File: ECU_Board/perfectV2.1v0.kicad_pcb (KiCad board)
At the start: 4 copper layers, 100 x 100 mm, 170 parts, among them IC1 Trig Cond Socket, IC2 Trig Cond Socket, J1 Conn_02x20_Odd_Even, J2 Conn_01x02, J3 MAP_Connector, J4 Conn_01x06, J5 Conn_01x05, J6 Conn_01x05, J8 Conn_01x04, Q1 SSM3K318R, Q2 SSM3K318R, Q3 SSM3K318R, U1 Teensy4.1, U10 LM324A, U11 LM324A, U12 CD4504B, U13 CD4504B, U14 CD4504B, U2 LM2576-5G, U3 SP720, U4 BM2LC105, U5 BM2LC105, U6 TC4424A, U7 TC4424A, U8 BM2LC105, U9 BM2LC105

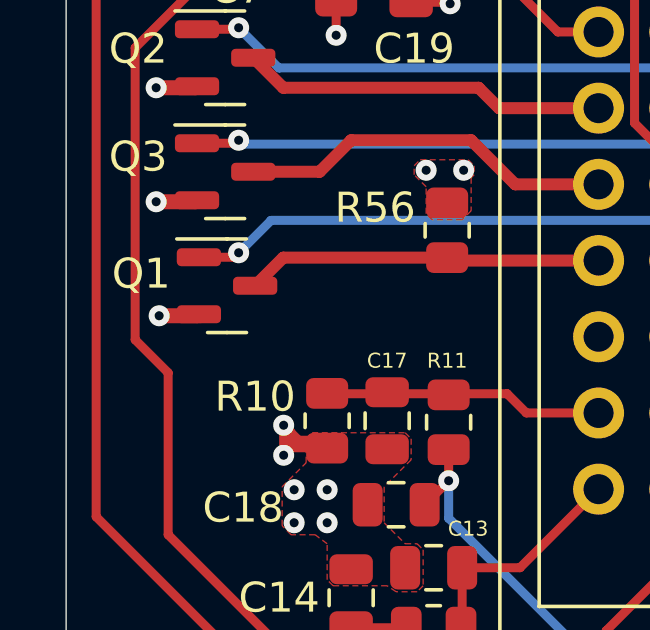
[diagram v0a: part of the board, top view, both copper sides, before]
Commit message: Changed Boost output to ACIS
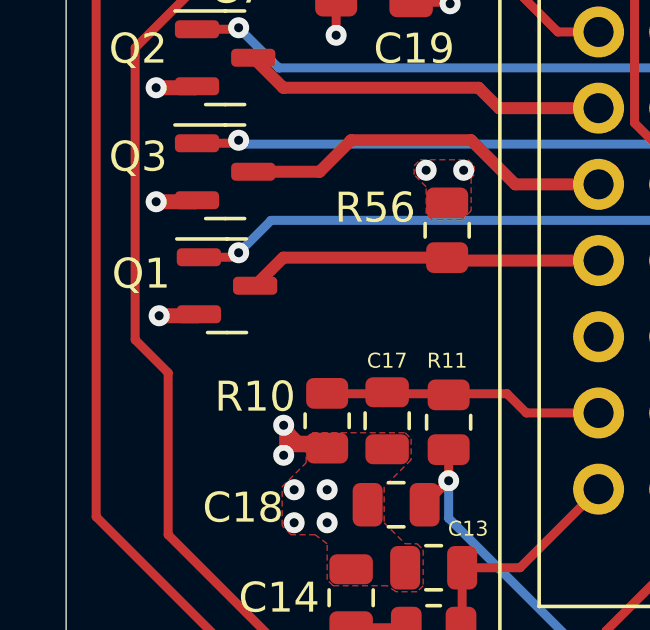
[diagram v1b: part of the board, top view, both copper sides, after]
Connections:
- net BOOST-5V renamed ACIS-5V
- net BOOST-OUT renamed ACIS-OUT
- net MCU-BOOST renamed MCU-ACIS
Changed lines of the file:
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@@
   (net 19 "BAT-5V")
   (net 20 "IDLE-OUT")
-  (net 21 "BOOST-OUT")
+  (net 21 "ACIS-OUT")
   (net 22 "CLT-5V")
   (net 23 "FLEX-IN")
@@
   (net 102 "MCU-IGN3")
   (net 103 "Net-(R46-Pad2)")
-  (net 104 "BOOST-5V")
+  (net 104 "ACIS-5V")
   (net 105 "Net-(R49-Pad1)")
   (net 106 "Net-(JP1-Pad2)")
@@
   (net 128 "MCU-INJ3")
   (net 129 "unconnected-(U1-Pad15)")
-  (net 130 "MCU-BOOST")
+  (net 130 "MCU-ACIS")
   (net 131 "unconnected-(U1-Pad18)")
   (net 132 "MCU-IDLE")
@@
       (net 2 "+12V") (pinfunction "K") (pintype "passive"))
     (pad "2" smd rect (at 1.65 0) (size 0.9 1.2) (layers "F.Cu" "F.Paste" "F.Mask")
-      (net 21 "BOOST-OUT") (pinfunction "A") (pintype "passive"))
+      (net 21 "ACIS-OUT") (pinfunction "A") (pintype "passive"))
     (model "${KICAD6_3DMODEL_DIR}/Diode_SMD.3dshapes/D_SOD-123.wrl"
       (offset (xyz 0 0 0))
@@
       (net 129 "unconnected-(U1-Pad15)") (pinfunction "3V3") (pintype "power_in+no_connect"))
     (pad "16" thru_hole circle (at 8.89 7.62 90) (size 1.6 1.6) (drill 1.1) (layers *.Cu *.Mask)
-      (net 130 "MCU-BOOST") (pinfunction "24_A10_TX6_SCL2") (pintype "bidirectional"))
+      (net 130 "MCU-ACIS") (pinfunction "24_A10_TX6_SCL2") (pintype "bidirectional"))
     (pad "17" thru_hole circle (at 11.43 7.62 90) (size 1.6 1.6) (drill 1.1) (layers *.Cu *.Mask)
       (net 79 "MCU-FAN") (pinfunction "25_A11_RX6_SDA2") (pintype "bidirectional"))
@@
       (net 105 "Net-(R49-Pad1)") (pintype "passive"))
     (pad "2" smd roundrect (at 0.51 0 270) (size 0.54 0.64) (layers "F.Cu" "F.Paste" "F.Mask") (roundrect_rratio 0.25)
-      (net 104 "BOOST-5V") (pintype "passive"))
+      (net 104 "ACIS-5V") (pintype "passive"))
     (model "${KICAD6_3DMODEL_DIR}/Resistor_SMD.3dshapes/R_0402_1005Metric.wrl"
       (offset (xyz 0 0 0))
@@
       (net 1 "GND") (pinfunction "SOURCE1") (pintype "input"))
     (pad "8" smd roundrect (at 2.625 -1.905 180) (size 1.65 0.6) (layers "F.Cu" "F.Paste" "F.Mask") (roundrect_rratio 0.25)
-      (net 21 "BOOST-OUT") (pinfunction "DRAIN1") (pintype "output"))
+      (net 21 "ACIS-OUT") (pinfunction "DRAIN1") (pintype "output"))
     (model "${KICAD6_3DMODEL_DIR}/Package_SO.3dshapes/SOP-8_3.9x4.9mm_P1.27mm.wrl"
       (offset (xyz 0 0 0))
@@
       (net 18 "INJ-4-OUT") (pinfunction "Pin_11") (pintype "passive"))
     (pad "12" thru_hole circle (at 2.54 12.7) (size 1.7 1.7) (drill 1) (layers *.Cu *.Mask)
-      (net 21 "BOOST-OUT") (pinfunction "Pin_12") (pintype "passive"))
+      (net 21 "ACIS-OUT") (pinfunction "Pin_12") (pintype "passive"))
     (pad "13" thru_hole circle (at 0 15.24) (size 1.7 1.7) (drill 1) (layers *.Cu *.Mask)
       (net 27 "IGN-1-OUT") (pinfunction "Pin_13") (pintype "passive"))
@@
       (net 33 "+3V3") (pinfunction "VCC") (pintype "power_in"))
     (pad "2" smd roundrect (at -2.8625 -1.625) (size 1.475 0.4) (layers "F.Cu" "F.Paste" "F.Mask") (roundrect_rratio 0.25)
-      (net 104 "BOOST-5V") (pinfunction "Aout") (pintype "output"))
+      (net 104 "ACIS-5V") (pinfunction "Aout") (pintype "output"))
     (pad "3" smd roundrect (at -2.8625 -0.975) (size 1.475 0.4) (layers "F.Cu" "F.Paste" "F.Mask") (roundrect_rratio 0.25)
-      (net 130 "MCU-BOOST") (pinfunction "Ain") (pintype "input"))
+      (net 130 "MCU-ACIS") (pinfunction "Ain") (pintype "input"))
     (pad "4" smd roundrect (at -2.8625 -0.325) (size 1.475 0.4) (layers "F.Cu" "F.Paste" "F.Mask") (roundrect_rratio 0.25)
       (net 85 "INJ1-5V") (pinfunction "Bout") (pintype "output"))
@@
     (fp_line (start -0.525 0.27) (end -0.525 -0.27) (layer "F.Fab") (width 0.1))
     (pad "1" smd roundrect (at -0.51 0 90) (size 0.54 0.64) (layers "F.Cu" "F.Paste" "F.Mask") (roundrect_rratio 0.25)
-      (net 104 "BOOST-5V") (pintype "passive"))
+      (net 104 "ACIS-5V") (pintype "passive"))
     (pad "2" smd roundrect (at 0.51 0 90) (size 0.54 0.64) (layers "F.Cu" "F.Paste" "F.Mask") (roundrect_rratio 0.25)
       (net 1 "GND") (pintype "passive"))
@@
   (segment (start 139 113.1) (end 139 111.45) (width 1) (layer "F.Cu") (net 1))
   (segment (start 88.21375 116.22) (end 87.22 116.22) (width 0.5) (layer "F.Cu") (net 1))
-  (segment (start 51.975 152.6) (end 51.925 152.55) (width 0.5) (layer "F.Cu") (net 1))
   (segment (start 74.75125 125.455) (end 75.80125 124.405) (width 0.3) (layer "F.Cu") (net 1))
   (segment (start 86.72 125.42) (end 86.7 125.4) (width 0.3) (layer "F.Cu") (net 1))

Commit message: Finished adapter board, slight changes to ECU
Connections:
- net FAN-OUT renamed HT-OUT
- net MCU-FAN renamed MCU-HT
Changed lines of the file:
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@@
   (net 77 "Net-(JP7-Pad3)")
   (net 78 "MCU-TACHO")
-  (net 79 "MCU-FAN")
-  (net 80 "FAN-OUT")
+  (net 79 "HT-OUT")
+  (net 80 "MCU-HT")
   (net 81 "FUELPUMP-OUT")
   (net 82 "MCU-PUMP")
@@
       (net 130 "MCU-ACIS") (pinfunction "24_A10_TX6_SCL2") (pintype "bidirectional"))
     (pad "17" thru_hole circle (at 11.43 7.62 90) (size 1.6 1.6) (drill 1.1) (layers *.Cu *.Mask)
-      (net 79 "MCU-FAN") (pinfunction "25_A11_RX6_SDA2") (pintype "bidirectional"))
+      (net 80 "MCU-HT") (pinfunction "25_A11_RX6_SDA2") (pintype "bidirectional"))
     (pad "18" thru_hole circle (at 13.97 7.62 90) (size 1.6 1.6) (drill 1.1) (layers *.Cu *.Mask)
       (net 131 "unconnected-(U1-Pad18)") (pinfunction "26_A12_MOSI1") (pintype "bidirectional+no_connect"))
@@
       (net 69 "VR1-") (pinfunction "Pin_28") (pintype "passive"))
     (pad "29" thru_hole circle (at 0 35.56) (size 1.7 1.7) (drill 1) (layers *.Cu *.Mask)
-      (net 80 "FAN-OUT") (pinfunction "Pin_29") (pintype "passive"))
+      (net 79 "HT-OUT") (pinfunction "Pin_29") (pintype "passive"))
     (pad "30" thru_hole circle (at 2.54 35.56) (size 1.7 1.7) (drill 1) (layers *.Cu *.Mask)
       (net 70 "VR2-") (pinfunction "Pin_30") (pintype "passive"))
@@
     (fp_line (start 0.65 1.45) (end -0.65 1.45) (layer "F.Fab") (width 0.1))
     (pad "1" smd roundrect (at -0.9375 -0.95) (size 1.475 0.6) (layers "F.Cu" "F.Paste" "F.Mask") (roundrect_rratio 0.25)
-      (net 79 "MCU-FAN") (pinfunction "G") (pintype "input"))
+      (net 80 "MCU-HT") (pinfunction "G") (pintype "input"))
     (pad "2" smd roundrect (at -0.9375 0.95) (size 1.475 0.6) (layers "F.Cu" "F.Paste" "F.Mask") (roundrect_rratio 0.25)
       (net 1 "GND") (pinfunction "S") (pintype "passive"))
     (pad "3" smd roundrect (at 0.9375 0) (size 1.475 0.6) (layers "F.Cu" "F.Paste" "F.Mask") (roundrect_rratio 0.25)
-      (net 80 "FAN-OUT") (pinfunction "D") (pintype "passive"))
+      (net 79 "HT-OUT") (pinfunction "D") (pintype "passive"))
     (model "${KICAD6_3DMODEL_DIR}/Package_TO_SOT_SMD.3dshapes/SOT-23.wrl"
       (offset (xyz 0 0 0))
@@
   (segment (start 114.125 98.5) (end 102.2 98.5) (width 0.3) (layer "B.Cu") (net 78))
   (segment (start 102.25 122.5) (end 102.25 125.5) (width 0.3) (layer "B.Cu") (net 78))
-  (segment (start 51.8625 143.05) (end 53.2 143.05) (width 0.3) (layer "F.Cu") (net 79))
-  (segment (start 53.2 143.05) (end 53.25 143) (width 0.3) (layer "F.Cu") (net 79))
-  (via (at 53.25 143) (size 0.7) (drill 0.3) (layers "F.Cu" "B.Cu") (net 79))
-  (segment (start 132.12 106.335) (end 134.5 108.715) (width 0.3) (layer "B.Cu") (net 79))
-  (segment (start 72.75 140.5) (end 115.5 140.5) (width 0.3) (layer "B.Cu") (net 79))
-  (segment (start 134.5 108.715) (end 134.5 139.75) (width 0.3) (layer "B.Cu") (net 79))
-  (segment (start 133.745 140.505) (end 134.5 139.75) (width 0.3) (layer "B.Cu") (net 79))
-  (segment (start 68.91 144.34) (end 72.75 140.5) (width 0.3) (layer "B.Cu") (net 79))
-  (segment (start 54.59 144.34) (end 68.91 144.34) (width 0.3) (layer "B.Cu") (net 79))
-  (segment (start 53.25 143) (end 54.59 144.34) (width 0.3) (layer "B.Cu") (net 79))
-  (segment (start 115.505 140.505) (end 133.745 140.505) (width 0.3) (layer "B.Cu") (net 79))
-  (segment (start 115.5 140.5) (end 115.505 140.505) (width 0.3) (layer "B.Cu") (net 79))
-  (segment (start 65.2475 145.68) (end 61.93 145.68) (width 0.4) (layer "F.Cu") (net 80))
-  (segment (start 54.7375 145) (end 53.7375 144) (width 0.4) (layer "F.Cu") (net 80))
-  (segment (start 61.25 145) (end 54.7375 145) (width 0.4) (layer "F.Cu") (net 80))
-  (segment (start 61.93 145.68) (end 61.25 145) (width 0.4) (layer "F.Cu") (net 80))
+  (segment (start 65.2475 145.68) (end 61.93 145.68) (width 0.4) (layer "F.Cu") (net 79))
+  (segment (start 54.7375 145) (end 53.7375 144) (width 0.4) (layer "F.Cu") (net 79))
+  (segment (start 61.25 145) (end 54.7375 145) (width 0.4) (layer "F.Cu") (net 79))
+  (segment (start 61.93 145.68) (end 61.25 145) (width 0.4) (layer "F.Cu") (net 79))
+  (segment (start 51.8625 143.05) (end 53.2 143.05) (width 0.3) (layer "F.Cu") (net 80))
+  (segment (start 53.2 143.05) (end 53.25 143) (width 0.3) (layer "F.Cu") (net 80))
+  (via (at 53.25 143) (size 0.7) (drill 0.3) (layers "F.Cu" "B.Cu") (net 80))
+  (segment (start 132.12 106.335) (end 134.5 108.715) (width 0.3) (layer "B.Cu") (net 80))
+  (segment (start 72.75 140.5) (end 115.5 140.5) (width 0.3) (layer "B.Cu") (net 80))
+  (segment (start 134.5 108.715) (end 134.5 139.75) (width 0.3) (layer "B.Cu") (net 80))
+  (segment (start 133.745 140.505) (end 134.5 139.75) (width 0.3) (layer "B.Cu") (net 80))
+  (segment (start 68.91 144.34) (end 72.75 140.5) (width 0.3) (layer "B.Cu") (net 80))
+  (segment (start 54.59 144.34) (end 68.91 144.34) (width 0.3) (layer "B.Cu") (net 80))
+  (segment (start 53.25 143) (end 54.59 144.34) (width 0.3) (layer "B.Cu") (net 80))
+  (segment (start 115.505 140.505) (end 133.745 140.505) (width 0.3) (layer "B.Cu") (net 80))
+  (segment (start 115.5 140.5) (end 115.505 140.505) (width 0.3) (layer "B.Cu") (net 80))
   (segment (start 61 146.75) (end 62.47 148.22) (width 0.4) (layer "F.Cu") (net 81))
   (segment (start 53.7375 147.8) (end 55.95 147.8) (width 0.4) (layer "F.Cu") (net 81))
